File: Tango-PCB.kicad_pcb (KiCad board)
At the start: 2 copper layers, 132 x 86 mm, 64 parts, among them J1 PMOD, J10 Screw_Terminal_01x03, J11 Screw_Terminal_01x03, J12 Screw_Terminal_01x03, J13 Screw_Terminal_01x03, J14 Screw_Terminal_01x03, J15 Screw_Terminal_01x03, J16 Screw_Terminal_01x03, J17 Screw_Terminal_01x03, J18 Screw_Terminal_01x03, J19 Screw_Terminal_01x03, J2 EXT, J20 Screw_Terminal_01x03, J21 Screw_Terminal_01x03, J22 PWR, J23 SENSPWR, J26 PMOD, J3 Screw_Terminal_01x04, J4 Screw_Terminal_01x04, J5 Screw_Terminal_01x04, J6 Screw_Terminal_01x04, J7 Screw_Terminal_01x04, J8 Screw_Terminal_01x04, J9 Screw_Terminal_01x03, U1 ULN2803A, U2 ULN2803A, U3 ULN2803A

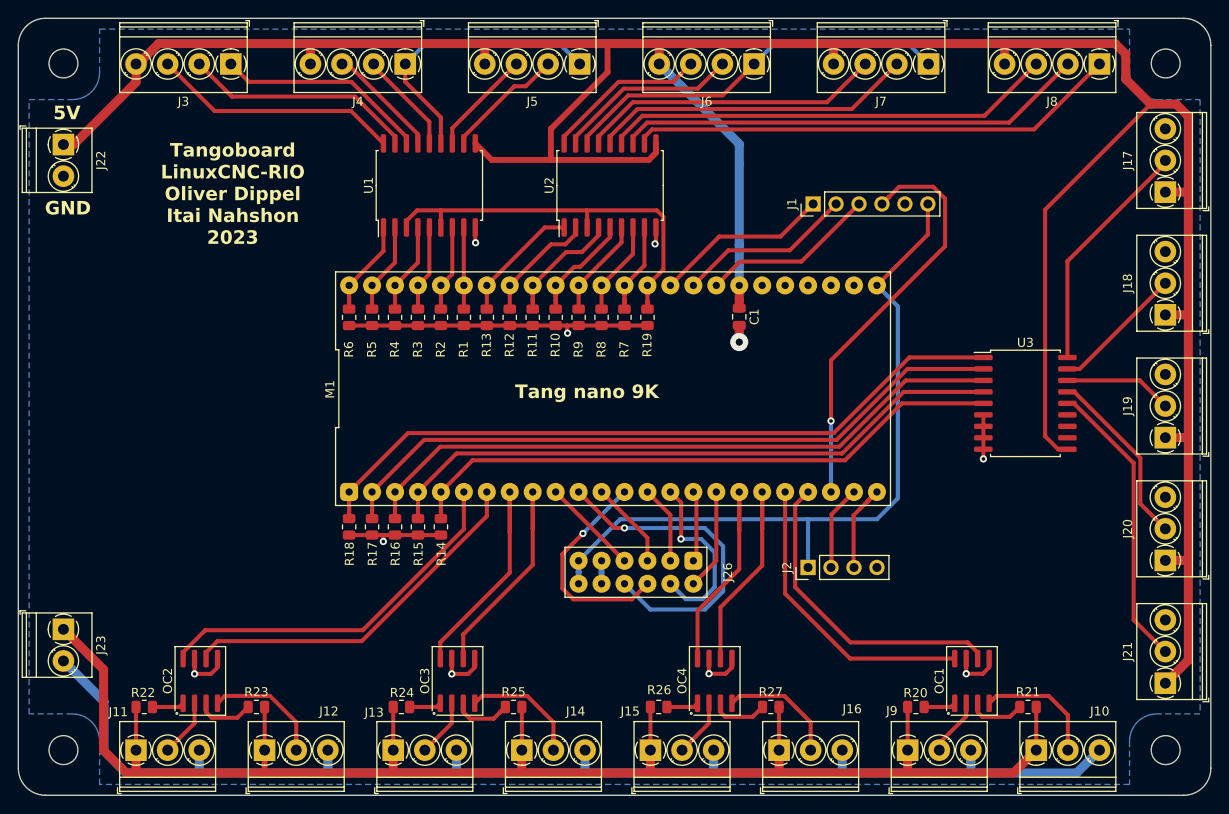
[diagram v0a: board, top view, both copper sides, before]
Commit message: Add SPI connector
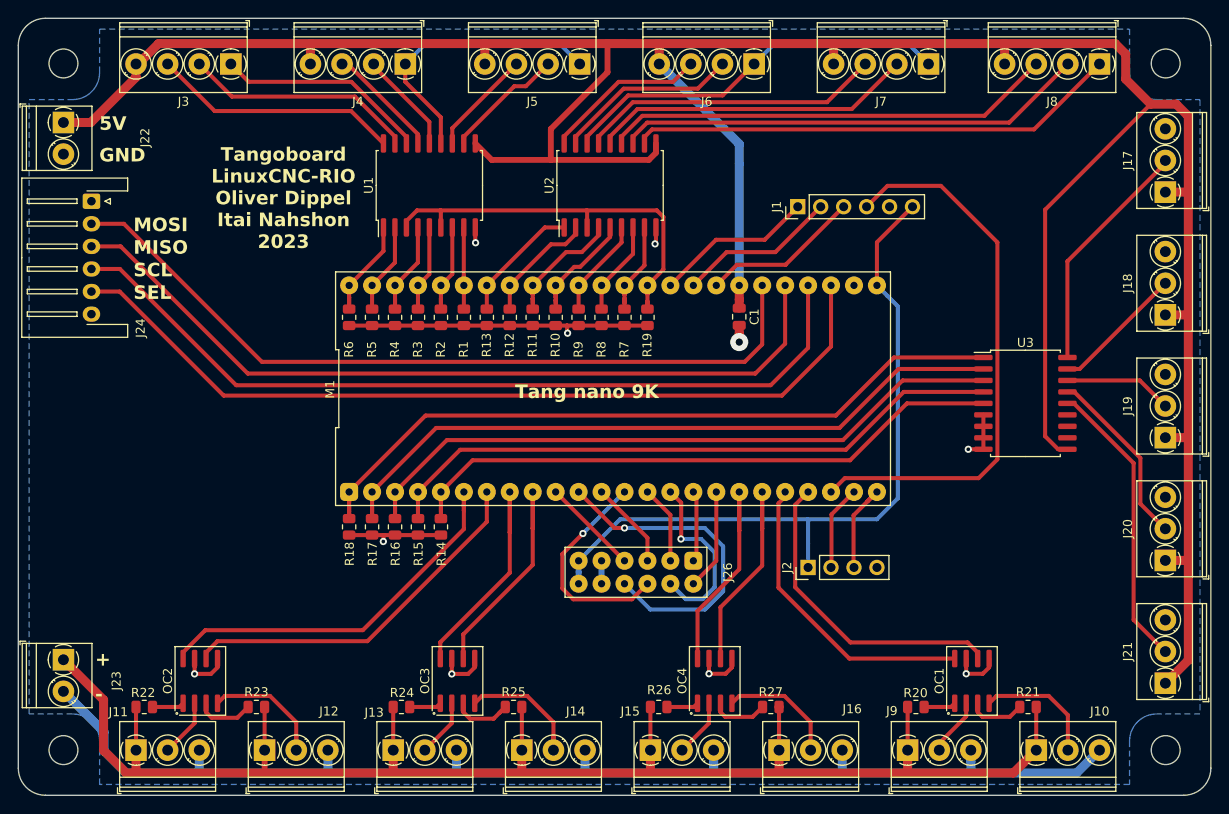
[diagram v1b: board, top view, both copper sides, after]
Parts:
- added J24: SPI, Connector_JST:JST_XH_S6B-XH-A-1_1x06_P2.50mm_Horizontal, F.Cu at (90.6, 75.7)
- moved J23 3.37 mm to (87.5, 126.5)
- moved J22 2.44 mm to (87.5, 67.0)
- moved J1 1.73 mm to (168.8, 76.4)
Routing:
- net /32: track 0.00 -> 95.6 mm
- net /31: track 0.00 -> 93.3 mm
- net /49: track 0.00 -> 90.4 mm
- net /48: track 0.00 -> 87.9 mm
- net /57: track 47.6 -> 62.0 mm, vias 1 -> 0
- net /5V: track 341.0 -> 334.3 mm
- net /SENS_V: track 179.0 -> 175.6 mm
- net /SENS_GND: track 142.1 -> 138.7 mm
- net /71: track 19.5 -> 17.7 mm
- net /72: track 19.5 -> 17.7 mm
- net /70: track 19.5 -> 17.7 mm
- net /3V3: track 83.2 -> 82.2 mm
- net /55: track 33.5 -> 34.2 mm
- net /GND: track 85.9 -> 86.5 mm
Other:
- board text added: "+"
- board text added: "-"
- board text added: "MISO"
- board text added: "MOSI"
- board text added: "SCL"
- board text added: "SEL"

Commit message: V2 - Individually select inputs 5V or 24V. Select input resistor.
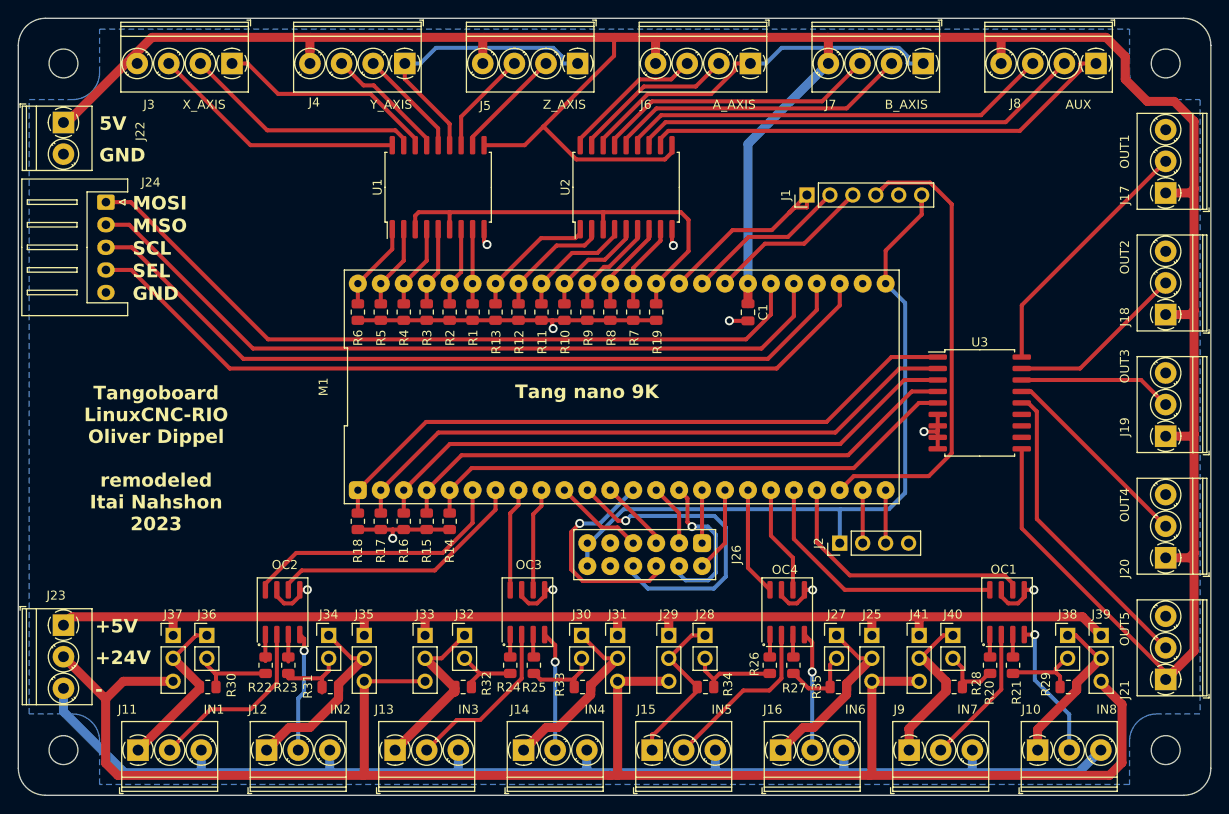
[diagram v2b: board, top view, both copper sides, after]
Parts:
- added J25: Sense Power Select, Connector_PinHeader_2.54mm:PinHeader_1x03_P2.54mm_Vertical, F.Cu at (177.0, 123.8)
- added J27: Led resistor select, Connector_PinHeader_2.54mm:PinHeader_1x02_P2.54mm_Vertical, F.Cu at (173.1, 123.8)
- added J28: Led resistor select, Connector_PinHeader_2.54mm:PinHeader_1x02_P2.54mm_Vertical, F.Cu at (158.5, 123.8)
- added J29: Sense Power Select, Connector_PinHeader_2.54mm:PinHeader_1x03_P2.54mm_Vertical, F.Cu at (154.5, 123.8)
- added J30: Led resistor select, Connector_PinHeader_2.54mm:PinHeader_1x02_P2.54mm_Vertical, F.Cu at (144.8, 123.8)
- added J31: Sense Power Select, Connector_PinHeader_2.54mm:PinHeader_1x03_P2.54mm_Vertical, F.Cu at (148.8, 123.8)
- added J32: Led resistor select, Connector_PinHeader_2.54mm:PinHeader_1x02_P2.54mm_Vertical, F.Cu at (131.9, 123.8)
- added J33: Sense Power Select, Connector_PinHeader_2.54mm:PinHeader_1x03_P2.54mm_Vertical, F.Cu at (127.5, 123.8)
- added J34: Led resistor select, Connector_PinHeader_2.54mm:PinHeader_1x02_P2.54mm_Vertical, F.Cu at (116.9, 123.8)
- added J35: Sense Power Select, Connector_PinHeader_2.54mm:PinHeader_1x03_P2.54mm_Vertical, F.Cu at (120.8, 123.8)
- added J36: Led resistor select, Connector_PinHeader_2.54mm:PinHeader_1x02_P2.54mm_Vertical, F.Cu at (103.4, 123.8)
- added J37: Sense Power Select, Connector_PinHeader_2.54mm:PinHeader_1x03_P2.54mm_Vertical, F.Cu at (99.6, 123.8)
- added J38: Led resistor select, Connector_PinHeader_2.54mm:PinHeader_1x02_P2.54mm_Vertical, F.Cu at (198.6, 123.8)
- added J39: Sense Power Select, Connector_PinHeader_2.54mm:PinHeader_1x03_P2.54mm_Vertical, F.Cu at (202.4, 123.8)
- added J40: Led resistor select, Connector_PinHeader_2.54mm:PinHeader_1x02_P2.54mm_Vertical, F.Cu at (185.9, 123.8)
- added J41: Sense Power Select, Connector_PinHeader_2.54mm:PinHeader_1x03_P2.54mm_Vertical, F.Cu at (182.2, 123.8)
- added R28: R, Resistor_SMD:R_0805_2012Metric, F.Cu at (186.1, 129.5)
- added R29: R, Resistor_SMD:R_0805_2012Metric, F.Cu at (198.7, 129.5)
- added R30: R, Resistor_SMD:R_0805_2012Metric, F.Cu at (103.5, 129.5)
- added R31: R, Resistor_SMD:R_0805_2012Metric, F.Cu at (117.0, 129.5)
- added R32: R, Resistor_SMD:R_0805_2012Metric, F.Cu at (131.7, 129.5)
- added R33: R, Resistor_SMD:R_0805_2012Metric, F.Cu at (145.0, 129.5)
- added R34: R, Resistor_SMD:R_0805_2012Metric, F.Cu at (158.6, 129.5)
- added R35: R, Resistor_SMD:R_0805_2012Metric, F.Cu at (173.3, 129.5)
- J10: value Screw_Terminal_01x03 -> IN8
- J11: value Screw_Terminal_01x03 -> IN1
- J12: value Screw_Terminal_01x03 -> IN2
- J13: value Screw_Terminal_01x03 -> IN3
- J14: value Screw_Terminal_01x03 -> IN4
- J15: value Screw_Terminal_01x03 -> IN5
- J16: value Screw_Terminal_01x03 -> IN6
- J17: value Screw_Terminal_01x03 -> OUT1
- J18: value Screw_Terminal_01x03 -> OUT2
- J19: value Screw_Terminal_01x03 -> OUT3
- J20: value Screw_Terminal_01x03 -> OUT4
- J21: value Screw_Terminal_01x03 -> OUT5
- J23: footprint TerminalBlock_Phoenix:TerminalBlock_Phoenix_PT-1,5-2-3.5-H_1x02_P3.50mm_Horizontal -> TerminalBlock_Phoenix:TerminalBlock_Phoenix_PT-1,5-3-3.5-H_1x03_P3.50mm_Horizontal
- J24: footprint Connector_JST:JST_XH_S6B-XH-A-1_1x06_P2.50mm_Horizontal -> Connector_JST:JST_XH_S5B-XH-A_1x05_P2.50mm_Horizontal
- J3: value Screw_Terminal_01x04 -> X_AXIS
- J4: value Screw_Terminal_01x04 -> Y_AXIS
- J5: value Screw_Terminal_01x04 -> Z_AXIS
- J6: value Screw_Terminal_01x04 -> A_AXIS
- J7: value Screw_Terminal_01x04 -> B_AXIS
- J8: value Screw_Terminal_01x04 -> AUX
- J9: value Screw_Terminal_01x03 -> IN7
- moved R22 14.2 mm to (109.9, 127.1), turned to -90 degrees
- moved R26 13.1 mm to (165.7, 127.1), turned to -90 degrees
- moved R24 12.9 mm to (136.9, 127.1), turned to -90 degrees
- moved OC2 11.9 mm to (111.8, 121.2)
- moved OC4 11.1 mm to (167.6, 121.2)
- moved OC3 10.8 mm to (138.9, 121.2)
- moved R20 9.42 mm to (190.1, 127.1), turned to -90 degrees
- moved OC1 8.54 mm to (191.9, 121.2)
- moved R23 5.82 mm to (112.4, 127.1), turned to -90 degrees
- moved R27 5.26 mm to (168.3, 127.1), turned to -90 degrees
- moved R25 5.14 mm to (139.6, 127.1), turned to -90 degrees
- moved U3 5.05 mm to (188.9, 98.1)
- moved R21 4.91 mm to (192.6, 127.1), turned to -90 degrees
- moved J2 4.42 mm to (173.4, 113.6)
- moved J23 3.83 mm to (87.5, 122.7)
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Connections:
- J10 pad 1: /SENS_V -> Net-(J10-Pin_1)
- J11 pad 1: /SENS_V -> Net-(J11-Pin_1)
- J12 pad 1: /SENS_V -> Net-(J12-Pin_1)
- J13 pad 1: /SENS_V -> Net-(J13-Pin_1)
- J14 pad 1: /SENS_V -> Net-(J14-Pin_1)
- J15 pad 1: /SENS_V -> Net-(J15-Pin_1)
- J16 pad 1: /SENS_V -> Net-(J16-Pin_1)
- J23 pad 1: /SENS_V -> /SENS_V2
- J23 pad 2: /SENS_GND -> /SENS_V1
- J24 pad 1: /GND -> /48
- J24 pad 2: /48 -> /49
- J24 pad 3: /49 -> /31
- J24 pad 4: /31 -> /32
- J24 pad 5: /32 -> /GND
- J9 pad 1: /SENS_V -> Net-(J9-Pin_1)
- R20 pad 2: /SENS_V -> Net-(J40-Pad2)
- R21 pad 2: /SENS_V -> Net-(J38-Pad2)
- R22 pad 2: /SENS_V -> Net-(J36-Pad2)
- R23 pad 2: /SENS_V -> Net-(J34-Pad2)
- R24 pad 2: /SENS_V -> Net-(J32-Pad2)
- R25 pad 2: /SENS_V -> Net-(J30-Pad2)
- R26 pad 2: /SENS_V -> Net-(J28-Pad2)
- R27 pad 2: /SENS_V -> Net-(J27-Pad2)
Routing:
- net /SENS_V1: track 0.00 -> 195.6 mm
- net /SENS_V: track 175.6 -> 0.00 mm
- net /SENS_V2: track 0.00 -> 131.6 mm
- net Net-(J12-Pin_1): track 0.00 -> 21.0 mm
- net Net-(J14-Pin_1): track 0.00 -> 20.3 mm
- net Net-(J16-Pin_1): track 0.00 -> 20.0 mm
- net Net-(J13-Pin_1): track 0.00 -> 19.8 mm
- net Net-(J15-Pin_1): track 0.00 -> 18.7 mm
- net Net-(J11-Pin_1): track 0.00 -> 18.6 mm
- net Net-(J10-Pin_1): track 0.00 -> 18.3 mm
- net Net-(J9-Pin_1): track 0.00 -> 18.0 mm
- net /28: track 26.1 -> 10.3 mm
- net /29: track 25.7 -> 10.3 mm
- net Net-(J11-Pin_2): track 6.42 -> 20.3 mm
- net /26: track 43.6 -> 30.0 mm
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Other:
- board text added: "+24V"
- board text added: "+5V"
- board text added: "Tangoboard LinuxCNC-RIO Oliver Dippel remodeled Itai Nahshon 2023"
- board text removed: "+"
- board text removed: "Tangoboard LinuxCNC-RIO Oliver Dippel Itai Nahshon 2023"

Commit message: Updates.
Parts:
- added C2: 100n, Capacitor_SMD:C_0805_2012Metric, F.Cu at (180.1, 116.5)
- added C3: 100n, Capacitor_SMD:C_0805_2012Metric, F.Cu at (146.4, 118.5)
- added C4: 100n, Capacitor_SMD:C_0805_2012Metric, F.Cu at (181.5, 78.1)
- C1: value C -> 100n
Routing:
- net /GND: track 79.2 -> 88.5 mm
- net /3V3: track 80.4 -> 88.6 mm
- net /SENS_GND: track 139.3 -> 143.2 mm
- net /72: track 21.8 -> 18.2 mm
- net /40: track 24.1 -> 26.4 mm
- net /32: track 91.0 -> 92.1 mm
- net /56: track 30.1 -> 30.8 mm
- net /31: track 89.0 -> 89.6 mm

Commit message: Update.
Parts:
- removed the R6 at (120.1, 88.0)
- removed REF1, REF2, REF3, REF4: MountingHole_3.2mm_M3, MountingHole:MountingHole_3.2mm_M3
- added H1: MountingHole, MountingHole:MountingHole_3.2mm_M3_Pad, F.Cu at (87.5, 60.5)
- added H2: MountingHole, MountingHole:MountingHole_3.2mm_M3_Pad, F.Cu at (87.5, 136.5)
- added H3: MountingHole, MountingHole:MountingHole_3.2mm_M3_Pad, F.Cu at (209.5, 60.5)
- added H4: MountingHole, MountingHole:MountingHole_3.2mm_M3_Pad, F.Cu at (209.5, 136.5)
- added R1: R, Resistor_SMD:R_0805_2012Metric, F.Cu at (120.1, 88.0)
- moved R2 30.5 mm to (122.6, 88.0)
- moved R3 25.4 mm to (153.1, 88.0)
- moved R4 2.54 mm to (125.2, 88.0)
- moved R5 2.54 mm to (127.7, 88.0)
- renumbered J22 to J1, J6 to J10, J7 to J11, J8 to J12, J17 to J13, J18 to J14, J19 to J15, J20 to J16, J21 to J17, J9 to J18, J10 to J19, J23 to J2, J11 to J20, J12 to J21, J13 to J22, J14 to J23, J15 to J24, J16 to J25, J40 to J26, J41 to J27, J38 to J28, J39 to J29, J2 to J3, J36 to J30, J37 to J31, J34 to J32, J35 to J33, J32 to J34, J33 to J35, J30 to J36, J31 to J37, J28 to J38, J29 to J39, J26 to J4, J27 to J40, J25 to J41, J1 to J5, J24 to J6, J3 to J7, J4 to J8, J5 to J9, R11 to R10, R10 to R11, R9 to R12, R8 to R13, R7 to R14, R18 to R15, R17 to R16, R16 to R17, R15 to R18, R14 to R19, R19 to R2, R28 to R21, R21 to R22, R29 to R23, R22 to R24, R30 to R25, R23 to R26, R31 to R27, R24 to R28, R32 to R29, R25 to R30, R33 to R31, R26 to R32, R34 to R33, R27 to R34, R5 to R4, R4 to R5, R2 to R6, R1 to R7, R13 to R8, R12 to R9
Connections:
- R2 pad 1: /73 -> /86
- R3 pad 1: /84 -> /73
- R4 pad 1: /86 -> /85
- R5 pad 1: /85 -> /84
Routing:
- net /3V3: track 88.6 -> 96.6 mm, vias 0 -> 1
- net /57: track 52.6 -> 54.9 mm
- net /GND: track 88.5 -> 87.9 mm
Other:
- board text added: "Tangoboard ITAI 2023"
- board text added: "Tangoboard LinuxCNC-RIO Oliver Dippel Remodeled Itai Nahshon 2023"
- board text removed: "Tangoboard LinuxCNC-RIO Oliver Dippel remodeled Itai Nahshon 2023"

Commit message: Update.
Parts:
- moved U3 4.83 mm to (193.7, 98.1)
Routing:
- net /5V: track 328.6 -> 387.0 mm
- net /3V3: track 96.6 -> 107.2 mm
- net /57: track 54.9 -> 63.0 mm
- net /39: track 63.6 -> 68.5 mm
- net Net-(J14-Pin_2): track 19.9 -> 15.0 mm
- net /38: track 72.8 -> 77.7 mm
- net /37: track 69.8 -> 74.6 mm
- net /36: track 66.7 -> 71.5 mm
- net /25: track 60.6 -> 65.4 mm
- net Net-(J15-Pin_2): track 17.1 -> 12.2 mm
- net Net-(J13-Pin_2): track 28.3 -> 25.8 mm
- net Net-(J17-Pin_2): track 34.1 -> 32.1 mm
- net Net-(J16-Pin_2): track 22.1 -> 20.3 mm
- net /31: track 89.6 -> 91.0 mm
- net /32: track 92.1 -> 93.5 mm
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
